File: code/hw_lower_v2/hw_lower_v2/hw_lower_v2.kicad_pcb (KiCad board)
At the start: 2 copper layers, 67 parts, among them Q1 BSS138, Q2 BSS138, Q3 BSS138, U2 BL0942, U3 DRV8220DRL, U4 TLV1805, U5 AMS1117, U6 AMS1117

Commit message: wip
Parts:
- added C14: 100n, Capacitor_SMD:C_0805_2012Metric, F.Cu at (27.2, 142.5)
- added D2: SMAJ5.0A, Diode_SMD:D_SMA, F.Cu at (18.9, 143.2)
- added K1: HE-S 2, multi_new:panasonic HE-s, F.Cu at (61.4, 85.4)
- added R10: 20K 1%, Resistor_SMD:R_1206_3216Metric, F.Cu at (51.7, 134.0)
- added R11: 20K 1%, Resistor_SMD:R_1206_3216Metric, F.Cu at (51.7, 137.3)
- added R17: TBD, Resistor_SMD:R_0603_1608Metric, F.Cu at (56.5, 123.8)
- added R30: 10K, Resistor_SMD:R_0603_1608Metric, F.Cu at (16.9, 146.8)
- added R7: 20K 1%, Resistor_SMD:R_1206_3216Metric, F.Cu at (51.7, 124.2)
- added R8: 20K 1%, Resistor_SMD:R_1206_3216Metric, F.Cu at (51.7, 127.5)
- added R9: 20K 1%, Resistor_SMD:R_1206_3216Metric, F.Cu at (51.7, 130.7)
- added U1: BRCS02C, multi_new:BRCS02C, F.Cu at (24.4, 114.7)
- C8: renamed from C5; value 100n 25V -> 100n
- C9: renamed from C6; value 100n 25V -> 100n
- R13: renamed from R9; value 20k -> 24R 0.1%
- R15: renamed from R33; value 20K -> TBD
- R16: renamed from R7; value 3K3 -> 1R6 0.1%
- R24: renamed from R11; value 20k -> 5k6
- R26: renamed from R12; value 20k -> 10k
- R29: renamed from R18; value R -> 1K
- R31: renamed from R22; value 200k -> 200k 1%
- R32: renamed from R23; value 66.5k -> 66.5k 1%
- R37: renamed from R39; value 160 -> 160R
- R38: renamed from R34; value DNP -> 75R
- R39: renamed from R35; value DNP -> 120R
- R40: renamed from R36; value DNP -> 39R
- R41: renamed from R37; value DNP -> 120R
- R42: renamed from R40; value 75 -> 75R
- R43: renamed from R38; value 510 -> 510R
- renumbered C8 to C1, C4 to C11, C11 to C4, C1 to C5, C2 to C6, D2 to D3, D3 to D6, Q3 to Q1, Q1 to Q3, R25 to R1, R10 to R12, R8 to R14, R6 to R18, R5 to R19, R26 to R2, R15 to R20, R13 to R21, R16 to R22, R14 to R23, R17 to R25, R32 to R27, R31 to R28, R27 to R3, R21 to R33, R24 to R34, R19 to R35, R20 to R36, R28 to R4, R29 to R5, R30 to R6, U5 to U6, U6 to U7
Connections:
- net /AC/AC_RELAY_PWM renamed Net-(Q1-G)
- net /AC/L_in renamed Net-(PS1-AC/L)
- PS1 pad 2: /AC/N_in -> Net-(PS1-AC/N)

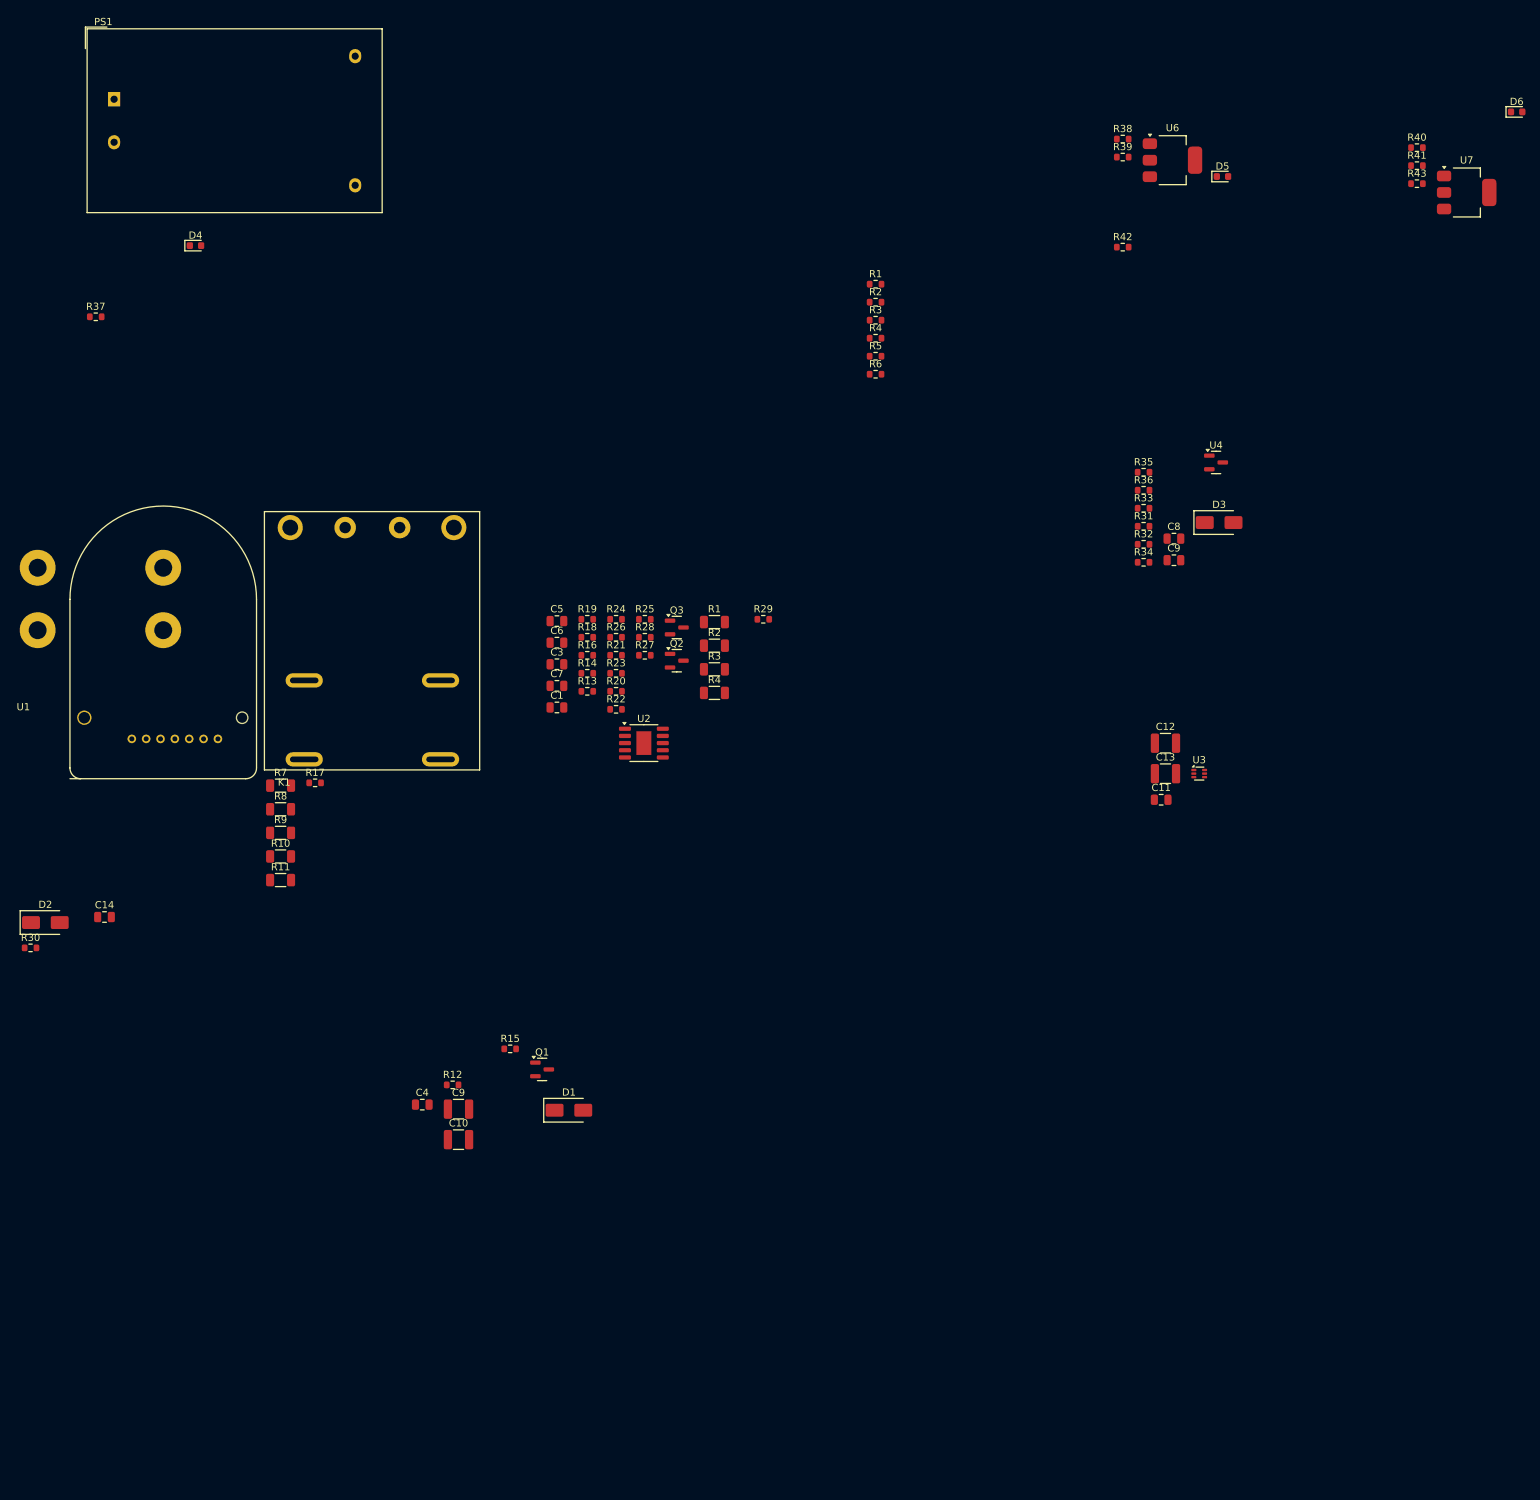
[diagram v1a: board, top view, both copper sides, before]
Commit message: finished schematic, started first pass of layout
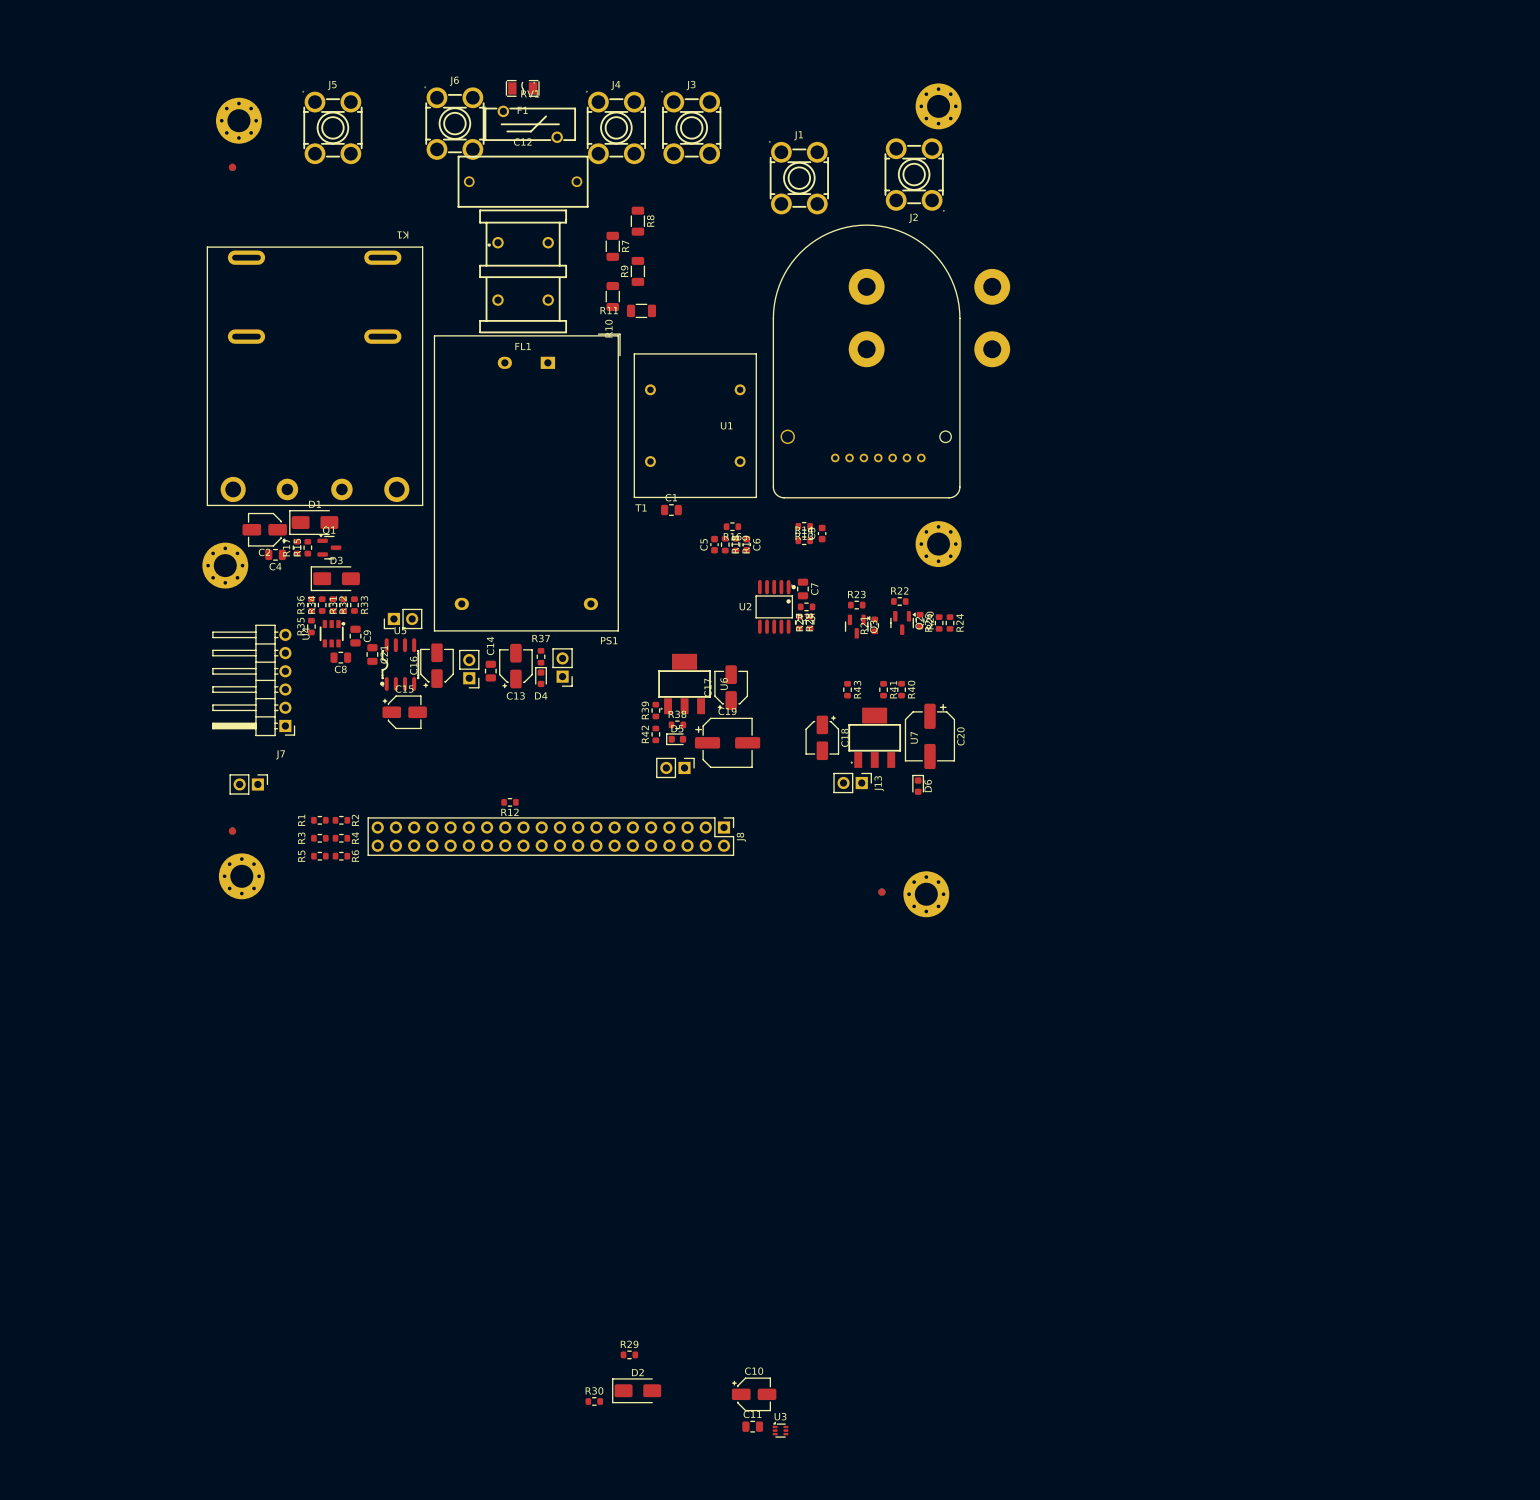
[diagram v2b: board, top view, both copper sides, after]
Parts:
- removed the C9 at (176.2, 92.8)
- removed the C9 at (76.5, 169.2)
- removed the R1 at (112.2, 101.4)
- removed the R1 at (134.6, 54.3)
- removed the R2 at (134.6, 56.8)
- removed the R2 at (112.2, 104.7)
- removed the R3 at (112.2, 108.0)
- removed the R3 at (134.6, 59.3)
- removed the R4 at (134.6, 61.8)
- removed the R4 at (112.2, 111.2)
- added C15: 10u, Capacitor_SMD:CP_Elec_4x5.4, F.Cu at (69.0, 113.9)
- added C16: 10u, Capacitor_SMD:CP_Elec_4x5.4, F.Cu at (73.5, 107.4)
- added C17: 10u, Capacitor_SMD:CP_Elec_4x5.4, F.Cu at (114.5, 110.5)
- added C18: 10u, Capacitor_SMD:CP_Elec_4x5.4, F.Cu at (127.2, 117.5)
- added C19: 100u, Capacitor_SMD:CP_Elec_6.3x5.4, F.Cu at (114.0, 118.2)
- added C2: 10u, Capacitor_SMD:CP_Elec_4x5.4, F.Cu at (49.5, 88.5)
- added C20: 100u, Capacitor_SMD:CP_Elec_6.3x5.4, F.Cu at (142.2, 117.3)
- added C21: 100n, Capacitor_SMD:C_0805_2012Metric, F.Cu at (64.5, 105.9)
- added C9: 100n, Capacitor_SMD:C_0805_2012Metric, F.Cu at (62.1, 103.3)
- added F1: 1A, JLCPCB:F1206, F.Cu at (85.4, 27.0)
- added FID1: Fiducial, Fiducial:Fiducial_1mm_Mask3mm, B.Cu at (45.0, 130.5)
- added FID2: Fiducial, Fiducial:Fiducial_1mm_Mask3mm, B.Cu at (45.0, 38.0)
- added FID3: Fiducial, Fiducial:Fiducial_1mm_Mask3mm, B.Cu at (135.5, 139.0)
- added FID4: Fiducial, Fiducial:Fiducial_1mm_Mask3mm, F.Cu at (45.0, 38.0)
- added FID5: Fiducial, Fiducial:Fiducial_1mm_Mask3mm, F.Cu at (135.5, 139.0)
- added FID6: Fiducial, Fiducial:Fiducial_1mm_Mask3mm, F.Cu at (45.0, 130.5)
- added FL1: Filter_EMI_CommonMode, JLCPCB:FILTER-TH_4P-L17.0-W12.0-P7.00-D0.6-S8.00, F.Cu at (85.5, 52.5)
- added H1: MountingHole_Pad, MountingHole:MountingHole_3.2mm_M3_Pad_Via, F.Cu at (143.4, 29.5)
- added H2: MountingHole_Pad, MountingHole:MountingHole_3.2mm_M3_Pad_Via, F.Cu at (45.9, 31.5)
- added H3: MountingHole_Pad, MountingHole:MountingHole_3.2mm_M3_Pad_Via, F.Cu at (143.4, 90.5)
- added H4: MountingHole_Pad, MountingHole:MountingHole_3.2mm_M3_Pad_Via, F.Cu at (44.0, 93.5)
- added H5: MountingHole_Pad, MountingHole:MountingHole_3.2mm_M3_Pad_Via, F.Cu at (141.7, 139.3)
- added H6: MountingHole_Pad, MountingHole:MountingHole_3.2mm_M3_Pad_Via, F.Cu at (46.3, 136.8)
- added J1: Screw_Terminal_01x01, JLCPCB:CONN-TH_T44001, F.Cu at (124.0, 39.5)
- added J10: Conn_01x02, Connector_PinHeader_2.54mm:PinHeader_1x02_P2.54mm_Vertical, F.Cu at (91.0, 109.0)
- added J11: Conn_01x02, Connector_PinHeader_2.54mm:PinHeader_1x02_P2.54mm_Vertical, F.Cu at (67.5, 100.9)
- added J12: Conn_01x02, Connector_PinHeader_2.54mm:PinHeader_1x02_P2.54mm_Vertical, F.Cu at (108.0, 121.7)
- added J13: Conn_01x02, Connector_PinHeader_2.54mm:PinHeader_1x02_P2.54mm_Vertical, F.Cu at (132.7, 123.8)
- added J14: Conn_01x02, Connector_PinHeader_2.54mm:PinHeader_1x02_P2.54mm_Vertical, F.Cu at (48.5, 124.0)
- added J2: Screw_Terminal_01x01, JLCPCB:CONN-TH_T44001, F.Cu at (140.0, 39.0)
- added J3: Screw_Terminal_01x01, JLCPCB:CONN-TH_T44001, F.Cu at (109.0, 32.5)
- added J4: Screw_Terminal_01x01, JLCPCB:CONN-TH_T44001, F.Cu at (98.5, 32.5)
- added J5: Screw_Terminal_01x01, JLCPCB:CONN-TH_T44001, F.Cu at (59.0, 32.5)
- added J6: Screw_Terminal_01x01, JLCPCB:CONN-TH_T44001, F.Cu at (76.0, 31.9)
- added J7: Conn_01x06_Pin, Connector_PinHeader_2.54mm:PinHeader_1x06_P2.54mm_Horizontal, F.Cu at (52.4, 115.8)
- added J8: Conn_02x20_Odd_Even, Connector_PinHeader_2.54mm:PinHeader_2x20_P2.54mm_Vertical, F.Cu at (113.5, 130.0)
- added J9: Conn_01x02, Connector_PinHeader_2.54mm:PinHeader_1x02_P2.54mm_Vertical, F.Cu at (78.0, 109.2)
- added R1: DNP, Resistor_SMD:R_0603_1608Metric, F.Cu at (57.2, 129.0)
- added R2: 100K, Resistor_SMD:R_0603_1608Metric, F.Cu at (60.2, 129.0)
- added R3: DNP, Resistor_SMD:R_0603_1608Metric, F.Cu at (57.2, 131.5)
- added R4: 100K, Resistor_SMD:R_0603_1608Metric, F.Cu at (60.2, 131.5)
- added RV1: 10D561K, JLCPCB:RES-TH_L12.5-W4.4-P7.50-D0.8-S3.60, F.Cu at (86.5, 32.0)
- added T1: TS3193-2C 2mA/2mA, multi_new:TS3193-2C, F.Cu at (109.5, 74.0)
- added U5: ICL7660A, JLCPCB:SOIC-8_L5.0-W4.0-P1.27-LS6.0-BL, F.Cu at (68.4, 107.3)
- C10, C13: value 22uF 25V -> 10u; footprint Capacitor_SMD:C_1210_3225Metric -> Capacitor_SMD:CP_Elec_4x5.4
- C12: value 22uF 25V -> 0.1uF/275Vac; footprint Capacitor_SMD:C_1210_3225Metric -> JLCPCB:CAP-TH_L18.0-W7.0-P15.00-D0.7
- C3, C5, C6: footprint Capacitor_SMD:C_0805_2012Metric -> Capacitor_SMD:C_0603_1608Metric
- D4, D5, D6: value LED -> RED LED
- K1: value HE-S 2 -> AHES4191
- R10, R11, R7, R8, R9: value 20K 1% -> 20K
- R15: value TBD -> 100k
- R16: value 1R6 0.1% -> 1R6 1%
- R17: value TBD -> 1K
- R24: value 5k6 -> 56k
- R26: value 10k -> 100k
- R35, R36: value 200K -> 100K
- U1: footprint multi_new:BRCS02C -> multi_new:BRCS02C_1
- U2: footprint Package_SO:SSOP-10-1EP_3.9x4.9mm_P1mm_EP2.1x3.3mm -> JLCPCB:SSOP-10_L4.9-W3.9-P1.00-LS6.0-BL
- U4: footprint Package_TO_SOT_SMD:SOT-23 -> JLCPCB:SOT-23-6_L2.9-W1.6-P0.95-LS2.8-BR
- U6, U7: footprint Package_TO_SOT_SMD:SOT-223-3_TabPin2 -> JLCPCB:SOT-223_L6.7-W3.5-P2.30-BR
- moved D6 125.6 mm to (140.6, 124.2), turned to -90 degrees
- moved U4 125.5 mm to (58.8, 103.0), turned to 90 degrees
- moved D3 123.2 mm to (59.5, 95.3)
- moved C12 118.9 mm to (85.5, 40.0)
- moved R35 118.0 mm to (56.0, 102.0), turned to 90 degrees
- moved C8 117.3 mm to (60.1, 106.3), turned to 180 degrees
- moved R36 117.1 mm to (56.0, 99.0), turned to 90 degrees
- moved R34 114.6 mm to (57.5, 99.0), turned to 90 degrees
- moved R32 113.3 mm to (59.0, 99.0), turned to -90 degrees
- moved U7 112.2 mm to (134.5, 117.5), turned to -90 degrees
- moved R31 112.0 mm to (60.5, 99.0), turned to 90 degrees
- moved R33 110.8 mm to (62.0, 99.0), turned to -90 degrees
- moved D5 109.2 mm to (107.0, 117.7)
- moved U3 108.6 mm to (121.4, 214.0)
- moved R43 106.2 mm to (130.7, 110.8), turned to -90 degrees
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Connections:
- C10 pad 2: Earth_Protective -> GND
- C12 pad 1: +12V -> Net-(C12-Pad1)
- C12 pad 2: GND -> /AC/N_in
